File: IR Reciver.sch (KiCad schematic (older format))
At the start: 13 parts

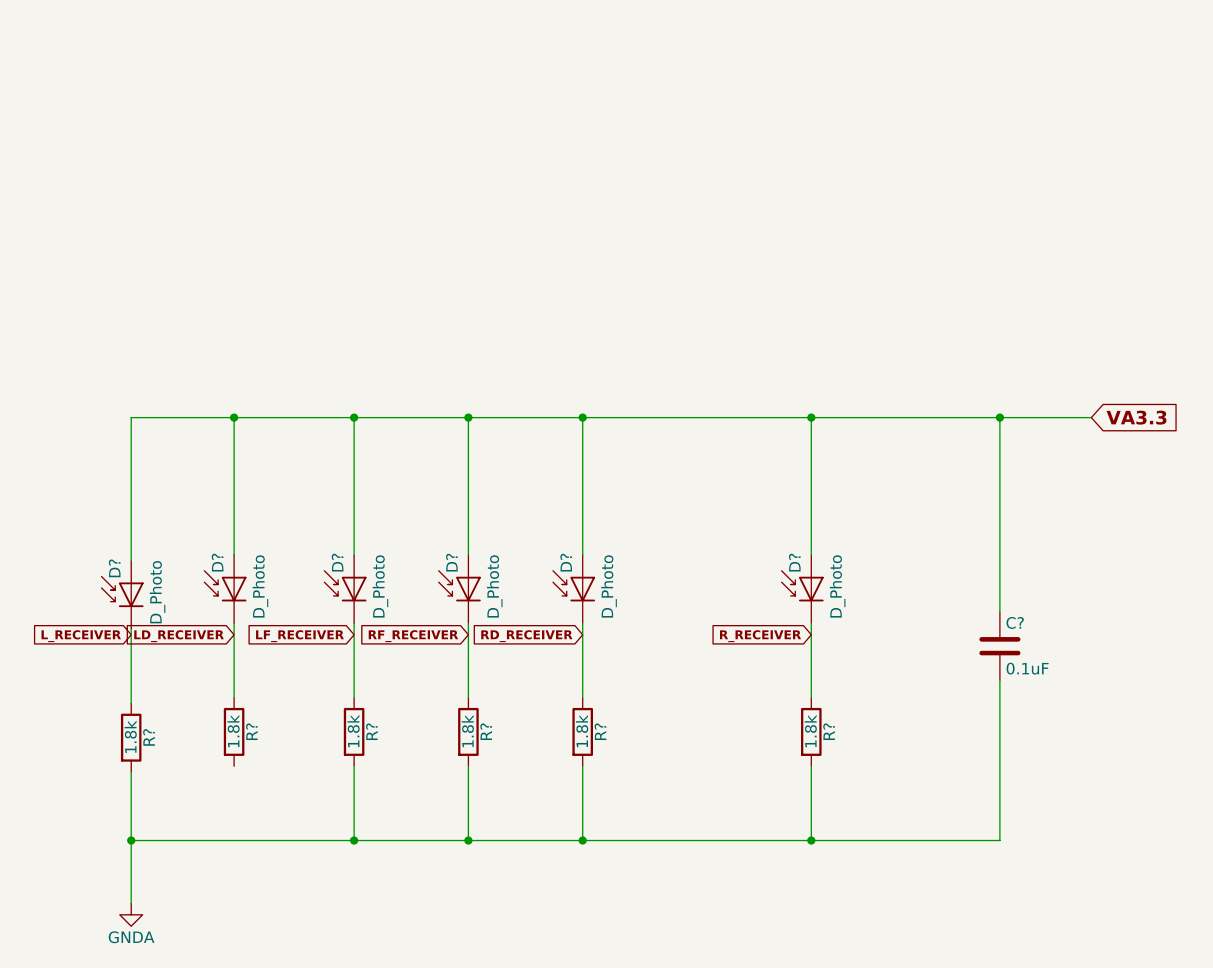
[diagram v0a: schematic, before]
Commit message: created footprint for linear requlator
added footprint for microcontroller linear requlator
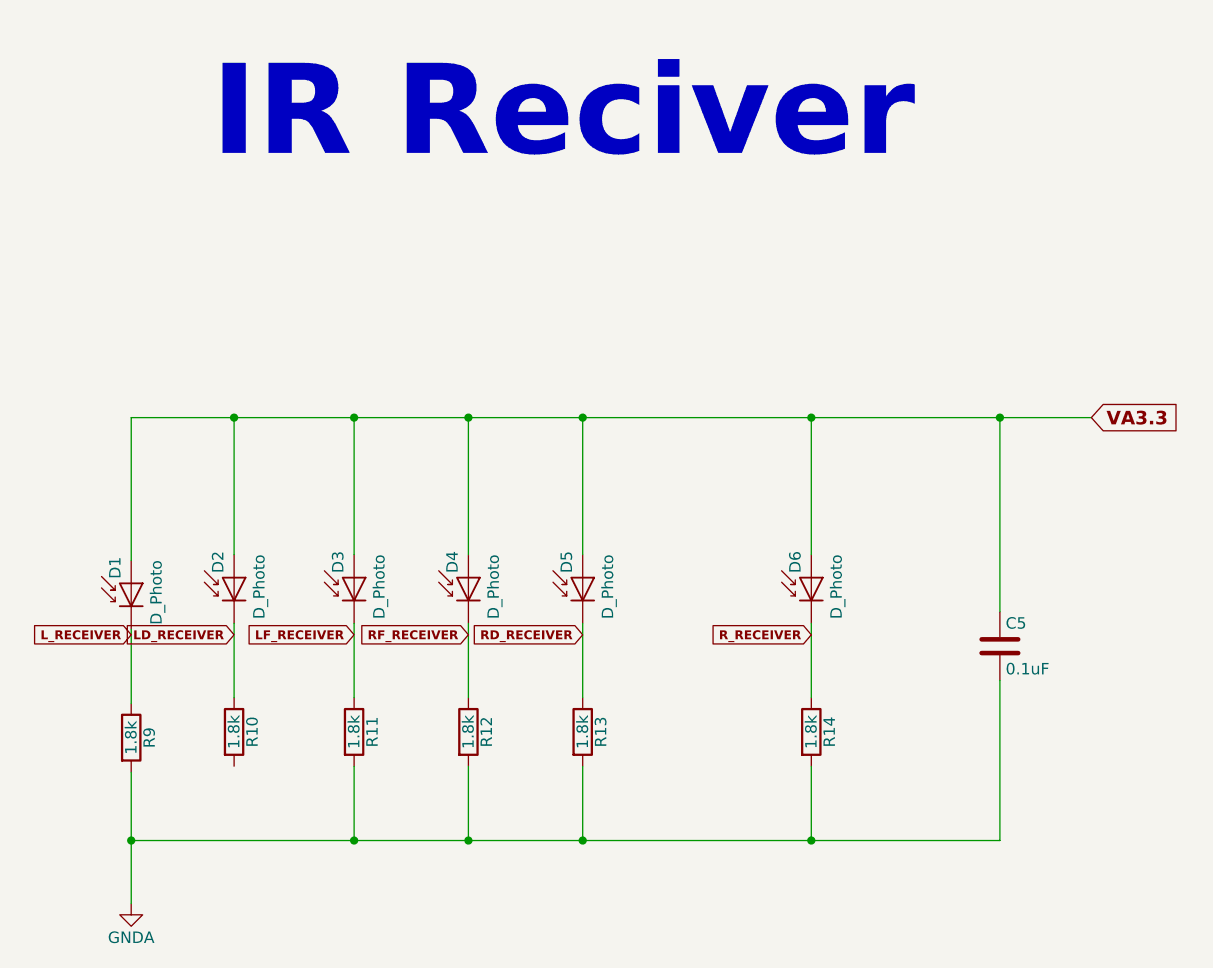
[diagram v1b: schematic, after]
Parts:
- C5: renamed from C?; footprint (none) -> Capacitors_SMD:C_0603
- D1, D2, D3, D4, D5, D6: renamed from D?; footprint (none) -> LEDs:LED_D3.0mm_Horizontal_O3.81mm_Z2.0mm
- R10, R11, R12, R13, R14, R9: renamed from R?; footprint (none) -> Resistors_SMD:R_0603
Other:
- note added: "IR Reciver"
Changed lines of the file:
@@
 $EndDescr
 $Comp
-L D_Photo D?
+L D_Photo D1
 U 1 1 5945F7BF
 P 3800 3125
-F 0 "D?" H 3820 3195 50  0000 L CNN
+F 0 "D1" H 3820 3195 50  0000 L CNN
 F 1 "D_Photo" H 3760 3015 50  0000 C CNN
-F 2 "" H 3750 3125 50  0001 C CNN
+F 2 "LEDs:LED_D3.0mm_Horizontal_O3.81mm_Z2.0mm" H 3750 3125 50  0001 C CNN
 F 3 "" H 3750 3125 50  0001 C CNN
 	1    3800 3125
@@
 $EndComp
 $Comp
-L R R?
+L R R9
 U 1 1 5945F8D6
 P 3800 3800
-F 0 "R?" V 3880 3800 50  0000 C CNN
+F 0 "R9" V 3880 3800 50  0000 C CNN
 F 1 "1.8k" V 3800 3800 50  0000 C CNN
-F 2 "" V 3730 3800 50  0001 C CNN
+F 2 "Resistors_SMD:R_0603" V 3730 3800 50  0001 C CNN
 F 3 "" H 3800 3800 50  0001 C CNN
 	1    3800 3800
@@
 	3800 3325 3800 3650
 $Comp
-L D_Photo D?
+L D_Photo D3
 U 1 1 5945FA4C
 P 4775 3100
-F 0 "D?" H 4795 3170 50  0000 L CNN
+F 0 "D3" H 4795 3170 50  0000 L CNN
 F 1 "D_Photo" H 4735 2990 50  0000 C CNN
-F 2 "" H 4725 3100 50  0001 C CNN
+F 2 "LEDs:LED_D3.0mm_Horizontal_O3.81mm_Z2.0mm" H 4725 3100 50  0001 C CNN
 F 3 "" H 4725 3100 50  0001 C CNN
 	1    4775 3100
@@
 $EndComp
 $Comp
-L R R?
+L R R11
 U 1 1 5945FA52
 P 4775 3775
-F 0 "R?" V 4855 3775 50  0000 C CNN
+F 0 "R11" V 4855 3775 50  0000 C CNN
 F 1 "1.8k" V 4775 3775 50  0000 C CNN
-F 2 "" V 4705 3775 50  0001 C CNN
+F 2 "Resistors_SMD:R_0603" V 4705 3775 50  0001 C CNN
 F 3 "" H 4775 3775 50  0001 C CNN
 	1    4775 3775
@@
 	4775 3300 4775 3625
 $Comp
-L D_Photo D?
+L D_Photo D5
 U 1 1 5945FADF
 P 5775 3100
-F 0 "D?" H 5795 3170 50  0000 L CNN
+F 0 "D5" H 5795 3170 50  0000 L CNN
 F 1 "D_Photo" H 5735 2990 50  0000 C CNN
-F 2 "" H 5725 3100 50  0001 C CNN
+F 2 "LEDs:LED_D3.0mm_Horizontal_O3.81mm_Z2.0mm" H 5725 3100 50  0001 C CNN
 F 3 "" H 5725 3100 50  0001 C CNN
 	1    5775 3100
@@
 $EndComp
 $Comp
-L R R?
+L R R13
 U 1 1 5945FAE5
 P 5775 3775
-F 0 "R?" V 5855 3775 50  0000 C CNN
+F 0 "R13" V 5855 3775 50  0000 C CNN
 F 1 "1.8k" V 5775 3775 50  0000 C CNN
-F 2 "" V 5705 3775 50  0001 C CNN
+F 2 "Resistors_SMD:R_0603" V 5705 3775 50  0001 C CNN
 F 3 "" H 5775 3775 50  0001 C CNN
 	1    5775 3775
@@
 	5775 3300 5775 3625
 $Comp
-L D_Photo D?
+L D_Photo D6
 U 1 1 5945FB3E
 P 6775 3100
-F 0 "D?" H 6795 3170 50  0000 L CNN
+F 0 "D6" H 6795 3170 50  0000 L CNN
 F 1 "D_Photo" H 6735 2990 50  0000 C CNN
-F 2 "" H 6725 3100 50  0001 C CNN
+F 2 "LEDs:LED_D3.0mm_Horizontal_O3.81mm_Z2.0mm" H 6725 3100 50  0001 C CNN
 F 3 "" H 6725 3100 50  0001 C CNN
 	1    6775 3100
@@
 $EndComp
 $Comp
-L R R?
+L R R14
 U 1 1 5945FB44
 P 6775 3775
-F 0 "R?" V 6855 3775 50  0000 C CNN
+F 0 "R14" V 6855 3775 50  0000 C CNN
 F 1 "1.8k" V 6775 3775 50  0000 C CNN
-F 2 "" V 6705 3775 50  0001 C CNN
+F 2 "Resistors_SMD:R_0603" V 6705 3775 50  0001 C CNN
 F 3 "" H 6775 3775 50  0001 C CNN
 	1    6775 3775
@@
 	6775 3300 6775 3625
 $Comp
-L C C?
+L C C5
 U 1 1 5945FE6A
 P 7600 3400
-F 0 "C?" H 7625 3500 50  0000 L CNN
+F 0 "C5" H 7625 3500 50  0000 L CNN
 F 1 "0.1uF" H 7625 3300 50  0000 L CNN
-F 2 "" H 7638 3250 50  0001 C CNN
+F 2 "Capacitors_SMD:C_0603" H 7638 3250 50  0001 C CNN
 F 3 "" H 7600 3400 50  0001 C CNN
 	1    7600 3400
@@
 $EndComp
 $Comp
-L GNDA #PWR?
+L GNDA #PWR07
 U 1 1 5945FEE7
 P 3800 4525
-F 0 "#PWR?" H 3800 4275 50  0001 C CNN
+F 0 "#PWR07" H 3800 4275 50  0001 C CNN
 F 1 "GNDA" H 3800 4375 50  0000 C CNN
 F 2 "" H 3800 4525 50  0001 C CNN
@@
 Connection ~ 7600 2400
 $Comp
-L D_Photo D?
+L D_Photo D2
 U 1 1 594637C3
 P 4250 3100
-F 0 "D?" H 4270 3170 50  0000 L CNN
+F 0 "D2" H 4270 3170 50  0000 L CNN
 F 1 "D_Photo" H 4210 2990 50  0000 C CNN
-F 2 "" H 4200 3100 50  0001 C CNN
+F 2 "LEDs:LED_D3.0mm_Horizontal_O3.81mm_Z2.0mm" H 4200 3100 50  0001 C CNN
 F 3 "" H 4200 3100 50  0001 C CNN
 	1    4250 3100
@@
 $EndComp
 $Comp
-L R R?
+L R R10
 U 1 1 594637C9
 P 4250 3775
-F 0 "R?" V 4330 3775 50  0000 C CNN
+F 0 "R10" V 4330 3775 50  0000 C CNN
 F 1 "1.8k" V 4250 3775 50  0000 C CNN
-F 2 "" V 4180 3775 50  0001 C CNN
+F 2 "Resistors_SMD:R_0603" V 4180 3775 50  0001 C CNN
 F 3 "" H 4250 3775 50  0001 C CNN
 	1    4250 3775
@@
 	4250 3300 4250 3625
 $Comp
-L D_Photo D?
+L D_Photo D4
 U 1 1 59463894
 P 5275 3100
-F 0 "D?" H 5295 3170 50  0000 L CNN
+F 0 "D4" H 5295 3170 50  0000 L CNN
 F 1 "D_Photo" H 5235 2990 50  0000 C CNN
-F 2 "" H 5225 3100 50  0001 C CNN
+F 2 "LEDs:LED_D3.0mm_Horizontal_O3.81mm_Z2.0mm" H 5225 3100 50  0001 C CNN
 F 3 "" H 5225 3100 50  0001 C CNN
 	1    5275 3100
@@
 $EndComp
 $Comp
-L R R?
+L R R12
 U 1 1 5946389A
 P 5275 3775
-F 0 "R?" V 5355 3775 50  0000 C CNN
+F 0 "R12" V 5355 3775 50  0000 C CNN
 F 1 "1.8k" V 5275 3775 50  0000 C CNN
-F 2 "" V 5205 3775 50  0001 C CNN
+F 2 "Resistors_SMD:R_0603" V 5205 3775 50  0001 C CNN
 F 3 "" H 5275 3775 50  0001 C CNN
 	1    5275 3775
@@
 Text GLabel 6775 3350 0    39   Input ~ 8
 R_RECEIVER
+Text Notes 4150 1300 0    394  ~ 79
+IR Reciver
 $EndSCHEMATC

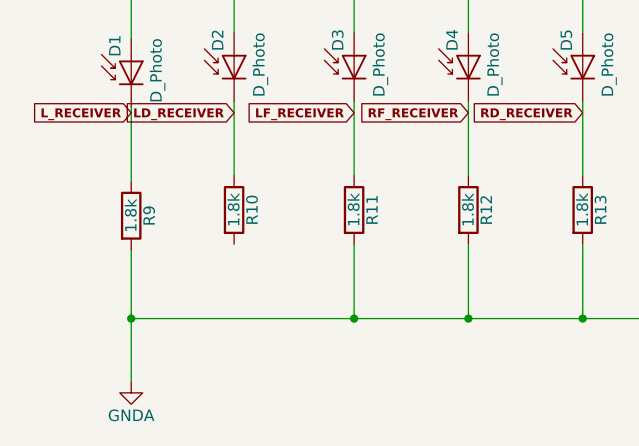
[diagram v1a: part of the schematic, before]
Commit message: fixed the mergre conflicts from the adding datasheet commite
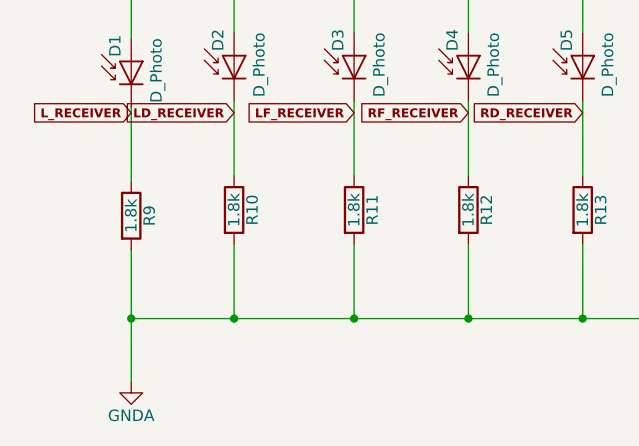
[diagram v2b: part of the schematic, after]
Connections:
- net GNDA: now also R10.2
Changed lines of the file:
@@
 Text Notes 4150 1300 0    394  ~ 79
 IR Reciver
+Wire Wire Line
+	4250 3925 4250 4250
+Connection ~ 4250 4250
 $EndSCHEMATC
